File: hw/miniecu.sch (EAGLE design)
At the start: 63 parts

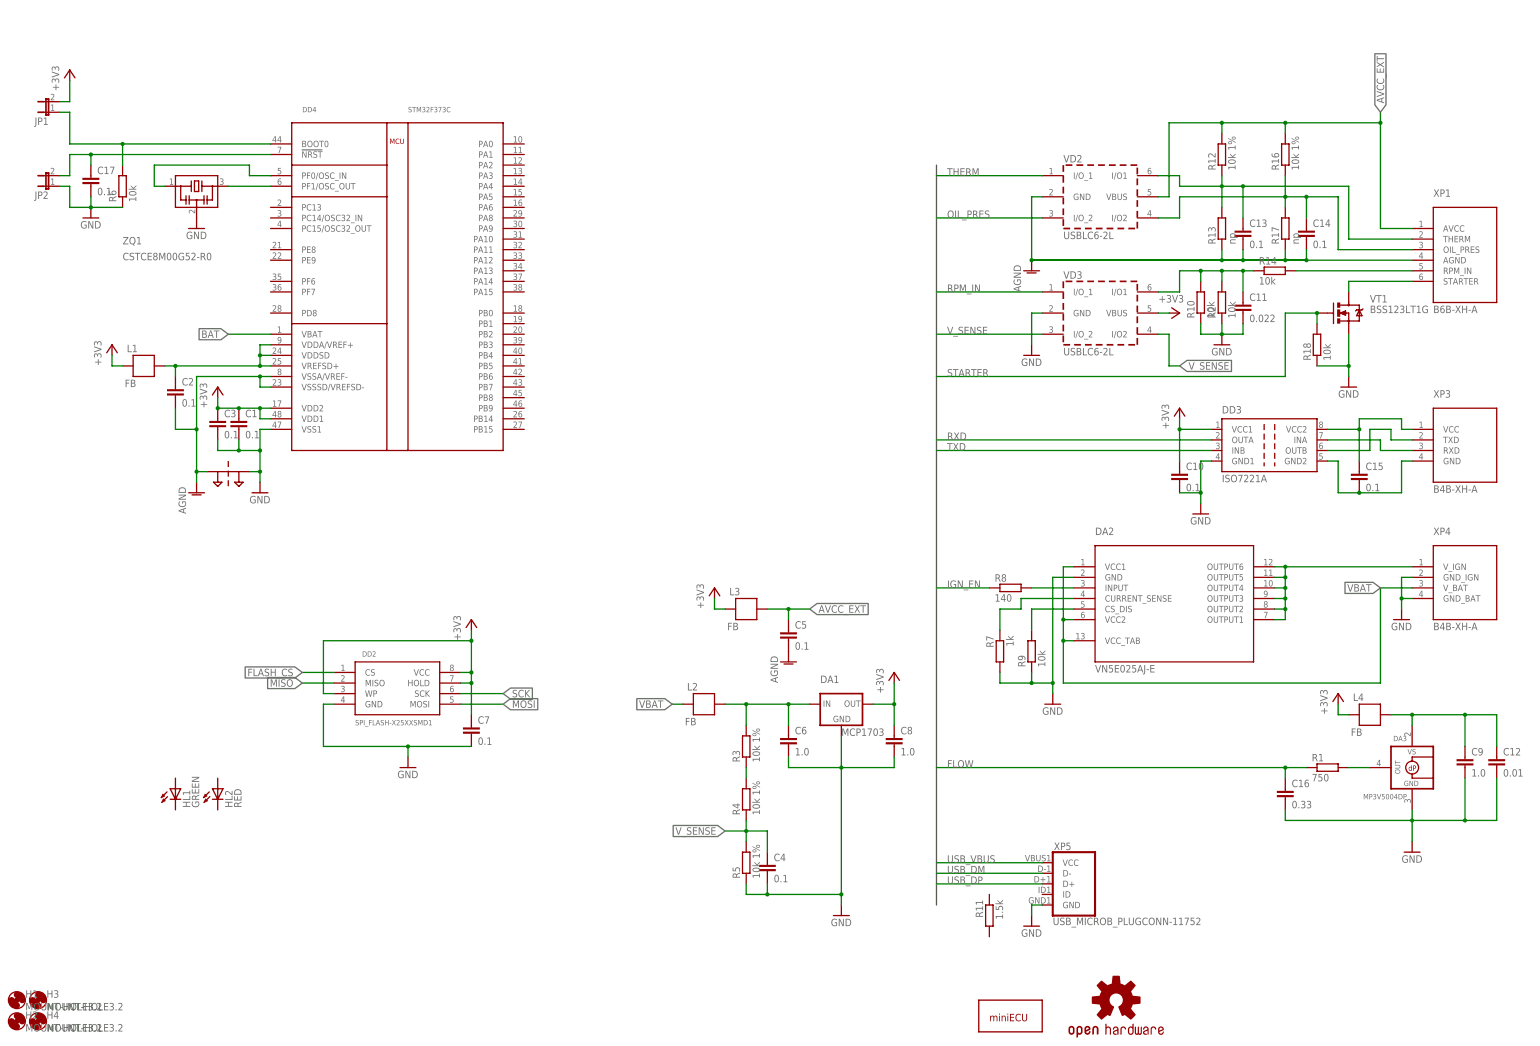
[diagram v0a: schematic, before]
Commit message: hw: do half connections of v2
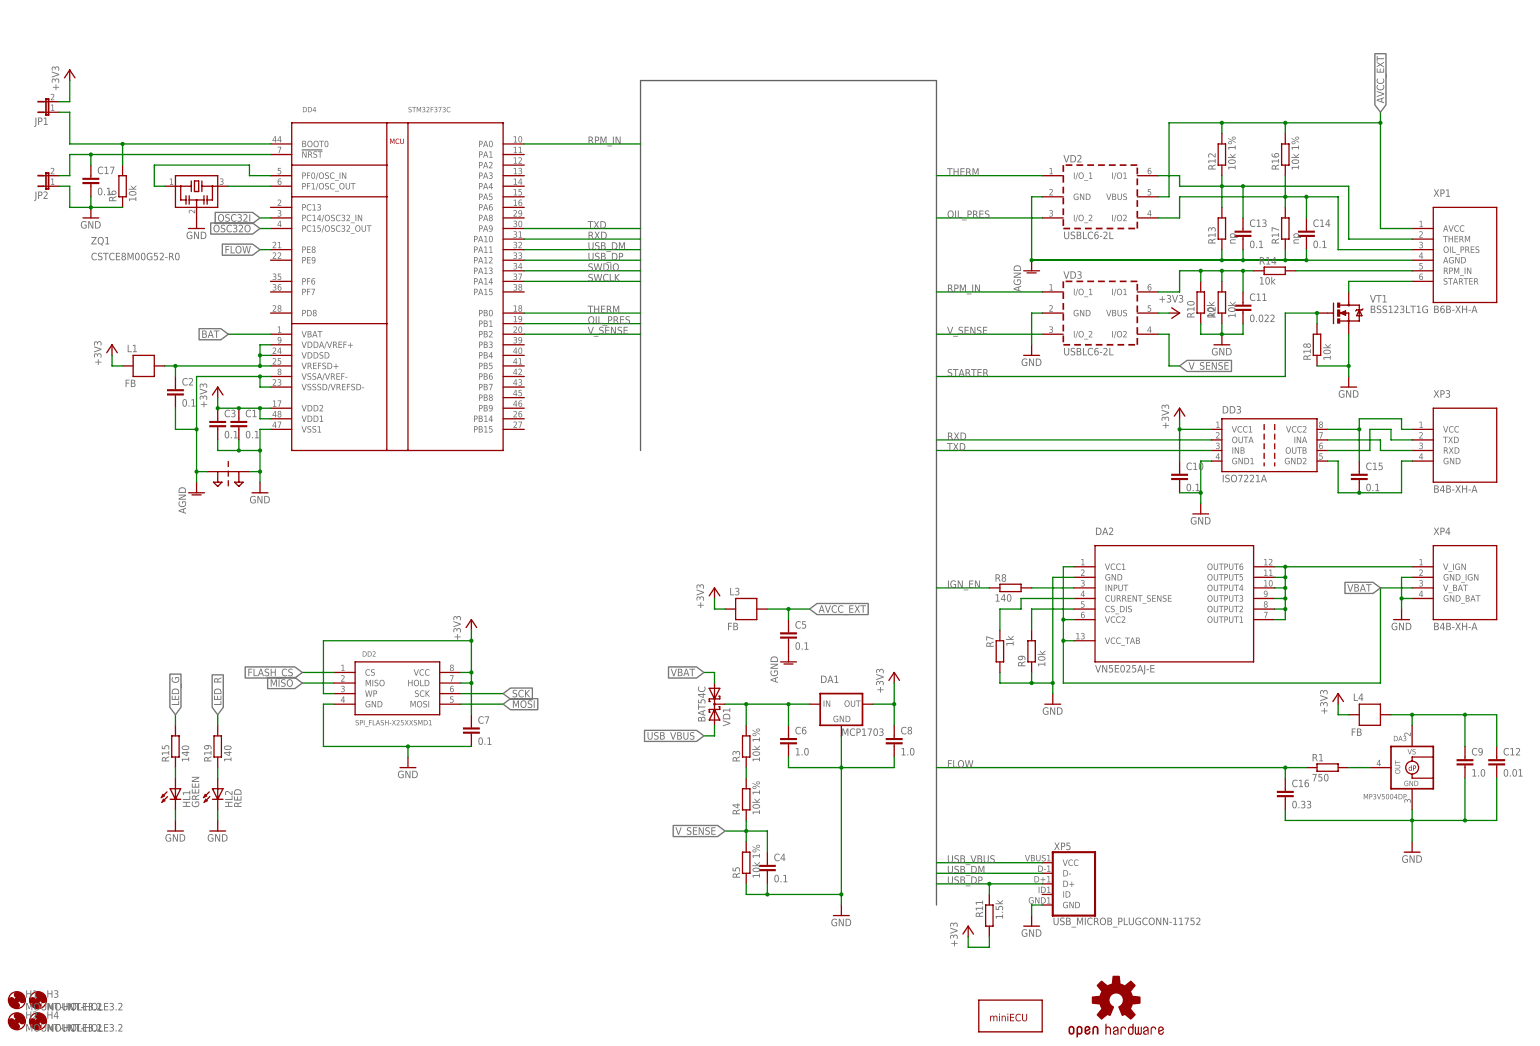
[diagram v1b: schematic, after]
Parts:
- removed L2: FB, SparkFun-Passives:FB
- added R15, R19: 140, resistor:R-EU_R0603
- added VD1: BAT54C, diode:BAT54C
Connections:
- new net LED_G: R15.2
- new net LED_R: R19.2
- new net N$12: HL2.A, R19.1
- new net N$8: HL1.A, R15.1
- new net OSC32I: DD4.PC14/OSC32_IN
- new net OSC32O: DD4.PC15/OSC32_OUT
- new net SWCLK: DD4.PA14
- new net SWDIO: DD4.PA13
- net +3V3: now also R11.2
- net FLOW: now also DD4.PE8
- net GND: now also HL1.C, HL2.C
- net N$6: now also VD1.CC; no longer L2.P$1
- net OIL_PRES: now also DD4.PB1
- net RPM_IN: now also DD4.PA0
- net RXD: now also DD4.PA10
- net THERM: now also DD4.PB0
- net TXD: now also DD4.PA9
- net USB_DM: now also DD4.PA11
- net USB_DP: now also DD4.PA12, R11.1
- net USB_VBUS: now also VD1.A2
- net VBAT: now also VD1.A1; no longer L2.P$2
- net V_SENSE: now also DD4.PB2

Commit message: hw: add SWD, EXT connectors; sch done
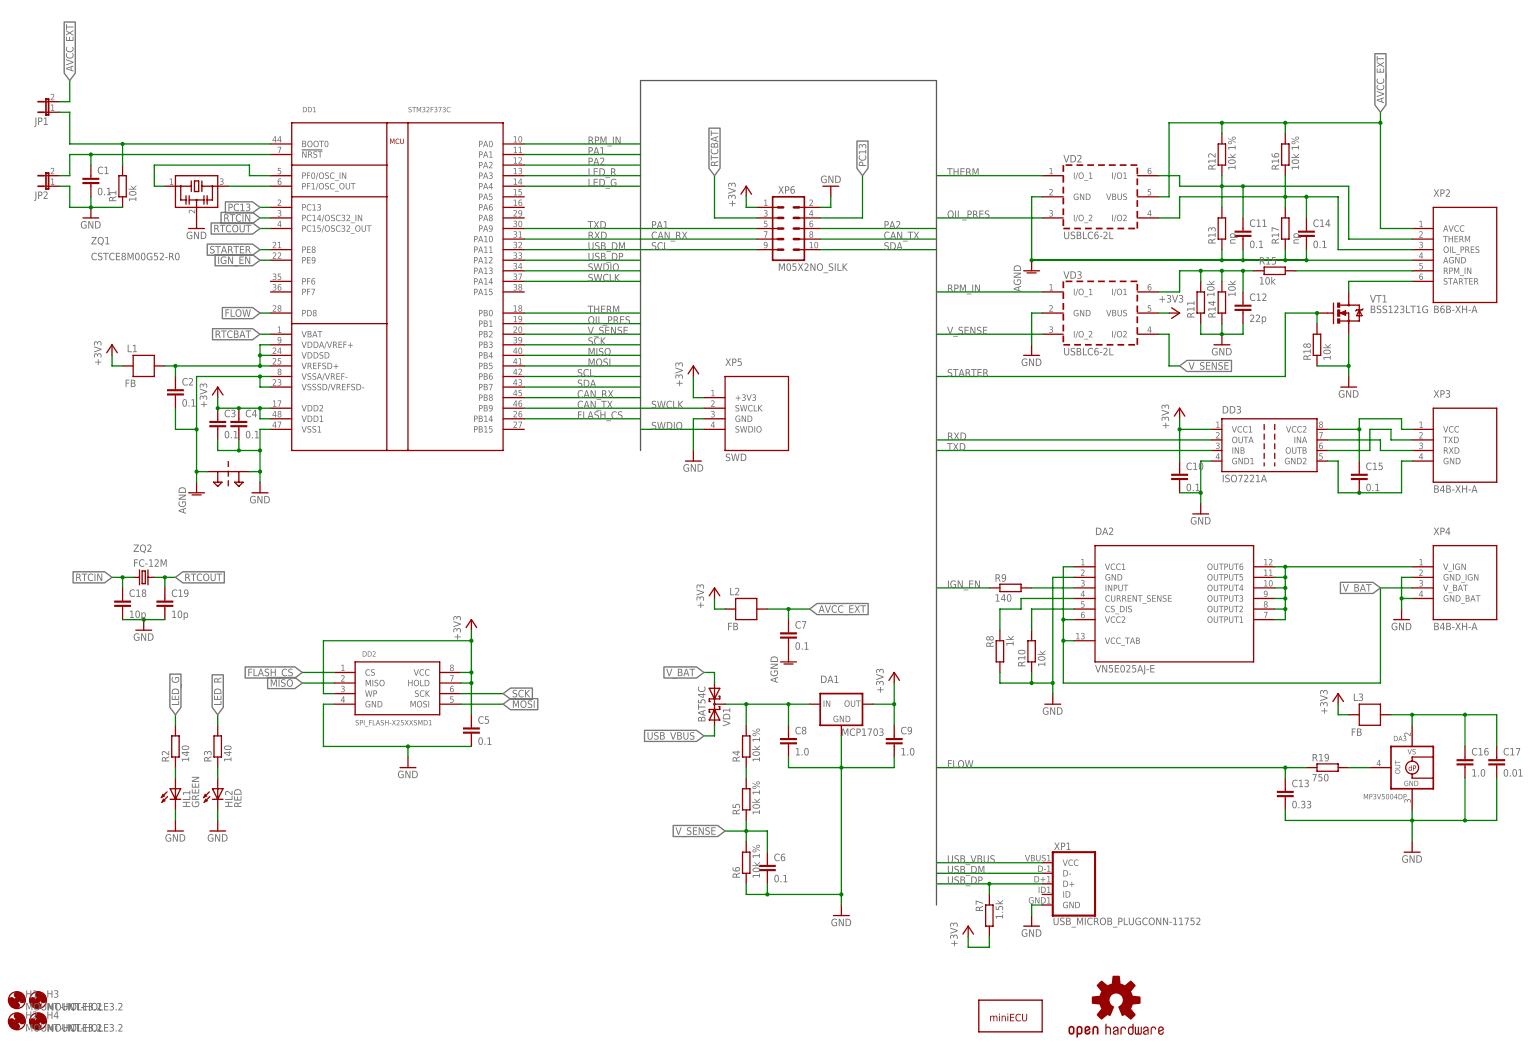
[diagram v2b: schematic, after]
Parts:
- removed L4: FB, SparkFun-Passives:FB
- added C18, C19: 10p, resistor:C-EUC0603
- added L2: FB, SparkFun-Passives:FB
- added XP2: B6B-XH-A, miniecu-con:SENSORS-B6B-XH-A
- added XP6: M05X2NO_SILK, SparkFun-Connectors:M05X2NO_SILK
- added ZQ2: FC-12M, crystal:FC-12M
- C11: value 0.022 -> 0.1
- C12: value 0.01 -> 22p
- C13: value 0.1 -> 0.33
- C16: value 0.33 -> 1.0; device resistor:C-EUC0603 -> resistor:C-EUC0805
- C17: value 0.1 -> 0.01
- C6: value 1.0 -> 0.1; device resistor:C-EUC0805 -> resistor:C-EUC0603
- LOGO1: value OSHW-LOGOL -> MINIECU_LOGO; device SparkFun-Aesthetics:OSHW-LOGOL -> miniecu:MINIECU_LOGO
- LOGO2: value MINIECU_LOGO -> OSHW-LOGOL; device miniecu:MINIECU_LOGO -> SparkFun-Aesthetics:OSHW-LOGOL
- R1: value 750 -> 10k
- R11: value 1.5k -> 10k
- R15: value 140 -> 10k
- R19: value 140 -> 750
- R2, R9: value 10k -> 140
- R3: value 10k 1% -> 140; device resistor:R-EU_R0805 -> resistor:R-EU_R0603
- R6: value 10k -> 10k 1%; device resistor:R-EU_R0603 -> resistor:R-EU_R0805
- R7: value 1k -> 1.5k
- R8: value 140 -> 1k
- XP1: value B6B-XH-A -> USB_MICROB_PLUGCONN-11752; device miniecu-con:SENSORS-B6B-XH-A -> SparkFun-Connectors:USB_MICROB_PLUGCONN-11752
- XP5: value USB_MICROB_PLUGCONN-11752 -> SWD; device SparkFun-Connectors:USB_MICROB_PLUGCONN-11752 -> miniecu-con:SWD
- renumbered DD4 to DD1
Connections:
- net N$5 renamed AVCC
- net VBAT renamed V_BAT
- removed net BAT: DD1.VBAT
- removed net N$10: C17.1, DD1.!NRST, JP2.2
- removed net N$11: DD1.BOOT0, JP1.1, R6.2
- removed net N$3: C12.1, C9.1, DA3.VS, L4.P$1
- removed net OSC32I: DD1.PC14/OSC32_IN
- removed net OSC32O: DD1.PC15/OSC32_OUT
- new net !NRST: C1.1, DD1.!NRST, JP2.2
- new net AVCC_FLOW: C16.1, C17.1, DA3.VS, L3.P$1
- new net BOOT0: DD1.BOOT0, JP1.1, R1.2
- new net CAN_RX: DD1.PB8, XP6.7
- new net CAN_TX: DD1.PB9, XP6.8
- new net PA1: DD1.PA1, XP6.5
- new net PA2: DD1.PA2, XP6.6
- new net PC13: DD1.PC13, XP6.4
- new net RTCBAT: DD1.VBAT, XP6.3
- new net RTCIN: C18.1, DD1.PC14/OSC32_IN, ZQ2.1
- new net RTCOUT: C19.1, DD1.PC15/OSC32_OUT, ZQ2.2
- new net SCL: DD1.PB6, XP6.9
- new net SDA: DD1.PB7, XP6.10
- net +3V3: now also C4.1, C5.1, C9.1, L2.P$2, R7.2, XP5.+3V3, XP6.1; no longer C1.1, C7.1, C8.1, JP1.2, L4.P$2, R11.2
- net AGND: now also C11.2, C7.2, XP2.AGND; no longer C13.2, C5.2, XP1.AGND
- net AVCC_EXT: now also C7.1, JP1.2, L2.P$1, XP2.AVCC; no longer C5.1, L3.P$1, XP1.AVCC
- net FLASH_CS: now also DD1.PB14
- net FLOW: now also C13.1, DD1.PD8, R19.1; no longer C16.1, DD1.PE8, R1.1
- net GND: now also C13.2, C18.2, C19.2, C5.2, R1.1, R11.1, R14.1, R8.2, XP1.GND, XP6.2; no longer C11.2, C7.2, R2.1, R5.1, R7.2, R9.1
- net IGN_EN: now also DD1.PE9, R9.1; no longer R8.1
- net LED_G: now also DD1.PA4, R2.2; no longer R15.2
- net LED_R: now also DD1.PA3, R3.2; no longer R19.2
- net MISO: now also DD1.PB4
- net MOSI: now also DD1.PB5
- net N$1: now also R4.1, R5.2; no longer R3.1, R4.2
- net N$12: now also R3.1; no longer R19.1
- net N$2: now also R8.1; no longer R7.1
- net N$4: now also R19.2; no longer R1.2
- net N$6: now also C8.1, R4.2; no longer C6.1, R3.2
- net N$7: now also R9.2; no longer R8.2
- net N$8: now also R2.1; no longer R15.1
- net N$9: now also R10.2; no longer R9.2
- net OIL_PRES: now also XP2.OIL_PRES; no longer XP1.OIL_PRES
- net RPM_IN: now also C12.1, R11.2, R14.2, R15.1; no longer C11.1, R10.2, R14.1, R2.2
- net RPM_IN_CON: now also R15.2, XP2.RPM_IN; no longer R14.2, XP1.RPM_IN
- net SCK: now also DD1.PB3
- net STARTER: now also DD1.PE8
- net STARTER_OUT: now also XP2.STARTER; no longer XP1.STARTER
- net SWCLK: now also XP5.SWCLK
- net SWDIO: now also XP5.SWDIO
- net THERM: now also C11.1, XP2.THERM; no longer C13.1, XP1.THERM
- net USB_DM: now also XP1.D-; no longer XP5.D-
- net USB_DP: now also R7.1, XP1.D+; no longer R11.1, XP5.D+
- net USB_VBUS: now also XP1.VCC; no longer XP5.VCC
- net V_SENSE: now also C6.1, R5.1, R6.2; no longer C4.1, R4.1, R5.2
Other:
- moved on the sheet: C1, C11, C12, C13, C16, C17, C4, C5, C6, C7, C8, C9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

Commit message: hw: route top half
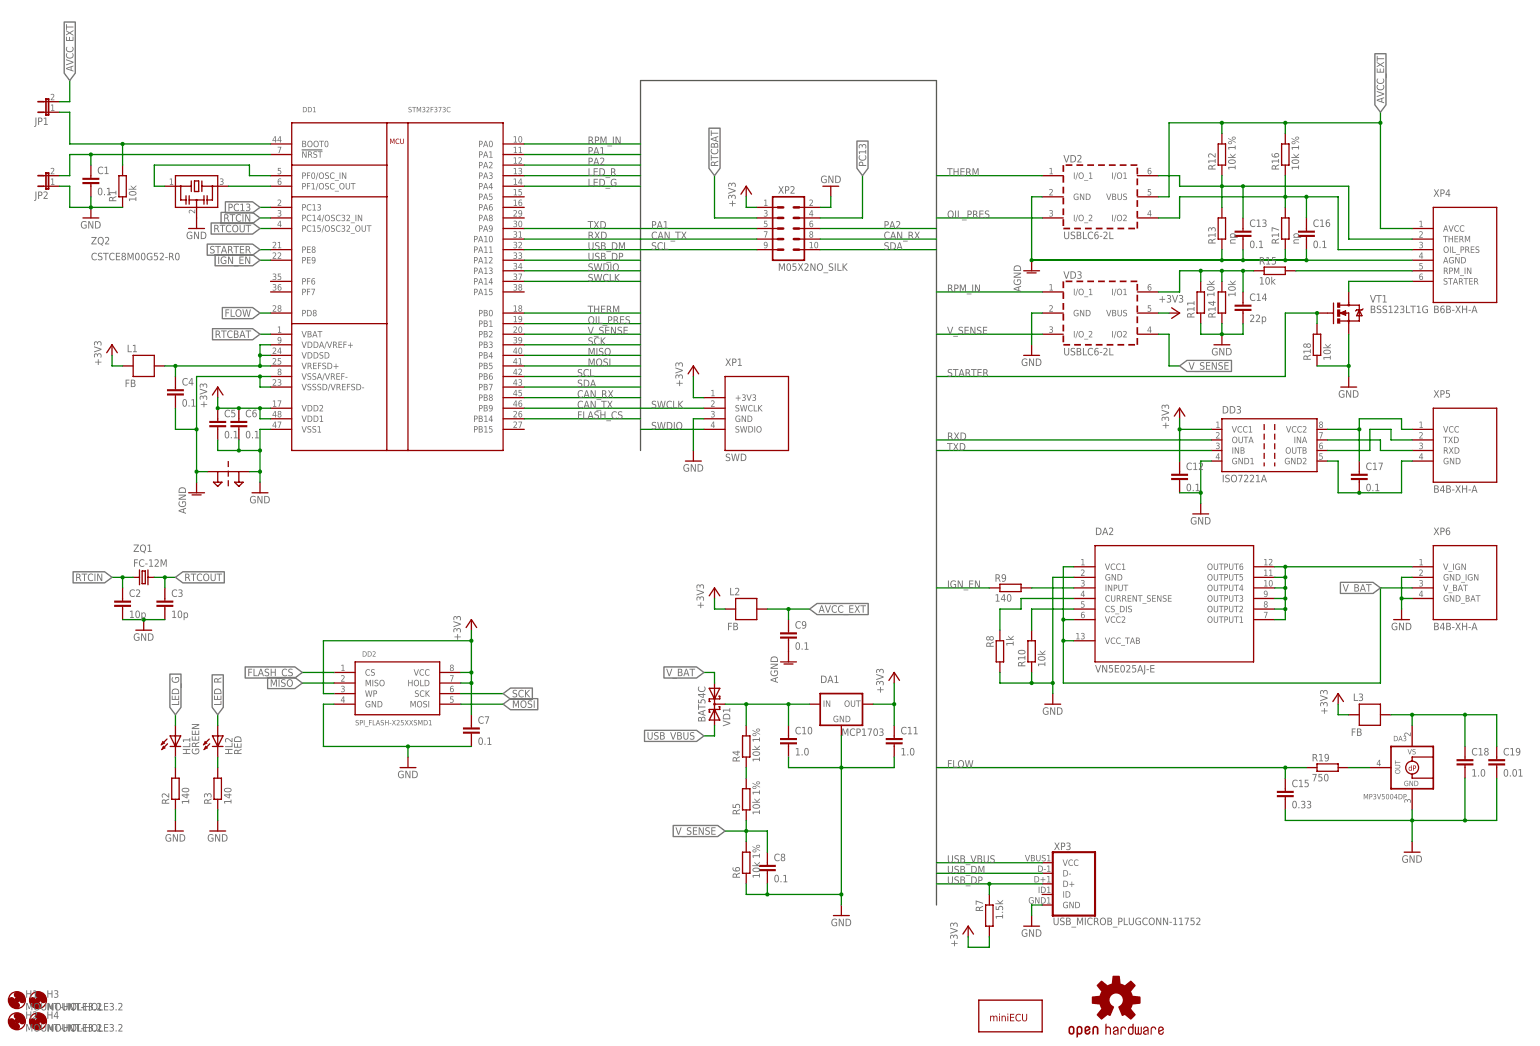
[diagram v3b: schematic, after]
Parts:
- C10, C11: value 0.1 -> 1.0; device resistor:C-EUC0603 -> resistor:C-EUC0805
- C12: value 22p -> 0.1
- C13: value 0.33 -> 0.1
- C14: value 0.1 -> 22p
- C15: value 0.1 -> 0.33
- C16, C8, C9: value 1.0 -> 0.1; device resistor:C-EUC0805 -> resistor:C-EUC0603
- C17: value 0.01 -> 0.1
- C18: value 10p -> 1.0; device resistor:C-EUC0603 -> resistor:C-EUC0805
- C19: value 10p -> 0.01
- C2, C3: value 0.1 -> 10p
- XP1: value USB_MICROB_PLUGCONN-11752 -> SWD; device SparkFun-Connectors:USB_MICROB_PLUGCONN-11752 -> miniecu-con:SWD
- XP2: value B6B-XH-A -> M05X2NO_SILK; device miniecu-con:SENSORS-B6B-XH-A -> SparkFun-Connectors:M05X2NO_SILK
- XP3: value B4B-XH-A -> USB_MICROB_PLUGCONN-11752; device miniecu-con:UART-B4B-XH-A -> SparkFun-Connectors:USB_MICROB_PLUGCONN-11752
- XP4: value B4B-XH-A -> B6B-XH-A; device miniecu-con:IGN_POWER-B4B-XH-A -> miniecu-con:SENSORS-B6B-XH-A
- XP5: value SWD -> B4B-XH-A; device miniecu-con:SWD -> miniecu-con:UART-B4B-XH-A
- XP6: value M05X2NO_SILK -> B4B-XH-A; device SparkFun-Connectors:M05X2NO_SILK -> miniecu-con:IGN_POWER-B4B-XH-A
- ZQ1: value CSTCE8M00G52-R0 -> FC-12M; device cstce-resonator:CSTCE8M00G52-R0 -> crystal:FC-12M
- ZQ2: value FC-12M -> CSTCE8M00G52-R0; device crystal:FC-12M -> cstce-resonator:CSTCE8M00G52-R0
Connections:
- removed net N$12: HL2.A, R3.1
- removed net N$8: HL1.A, R2.1
- new net N$3: HL2.C, R3.2
- new net N$5: HL1.C, R2.2
- net +3V3: now also C11.1, C12.1, C6.1, C7.1, XP1.+3V3, XP2.1; no longer C10.1, C3.1, C4.1, C9.1, XP5.+3V3, XP6.1
- net AGND: now also C13.2, C16.2, C4.2, C9.2, XP4.AGND; no longer C11.2, C14.2, C2.2, C7.2, XP2.AGND
- net AVCC: now also C4.1; no longer C2.1
- net AVCC_EXT: now also C9.1, XP4.AVCC; no longer C7.1, XP2.AVCC
- net AVCC_FLOW: now also C18.1, C19.1; no longer C16.1, C17.1
- net CAN_RX: now also XP2.8; no longer XP6.7
- net CAN_TX: now also XP2.7; no longer XP6.8
- net FLOW: now also C15.1; no longer C13.1
- net GND: now also C11.2, C14.2, C15.2, C2.2, C7.2, R2.1, R3.1, XP2.2, XP3.GND, XP6.GND_BAT, XP6.GND_IGN, ZQ2.2; no longer C13.2, C16.2, C17.2, C4.2, C9.2, HL1.C, HL2.C, XP4.GND_BAT, XP4.GND_IGN, XP5.GND, XP6.2, ZQ1.2
- net GND2: now also C17.2, XP5.GND; no longer C15.2, XP3.GND
- net IORXD: now also XP5.RXD; no longer XP3.RXD
- net IOTXD: now also XP5.TXD; no longer XP3.TXD
- net LED_G: now also HL1.A; no longer R2.2
- net LED_R: now also HL2.A; no longer R3.2
- net N$6: now also C10.1; no longer C8.1
- net OIL_PRES: now also C16.1, XP4.OIL_PRES; no longer C14.1, XP2.OIL_PRES
- net OSC_IN: now also ZQ2.1; no longer ZQ1.1
- net OSC_OUT: now also ZQ2.3; no longer ZQ1.3
- net PA1: now also XP2.5; no longer XP6.5
- net PA2: now also XP2.6; no longer XP6.6
- net PC13: now also XP2.4; no longer XP6.4
- net RPM_IN: now also C14.1; no longer C12.1
- net RPM_IN_CON: now also XP4.RPM_IN; no longer XP2.RPM_IN
- net RTCBAT: now also XP2.3; no longer XP6.3
- net RTCIN: now also C2.1, ZQ1.1; no longer C18.1, ZQ2.1
- net RTCOUT: now also C3.1, ZQ1.2; no longer C19.1, ZQ2.2
- net SCL: now also XP2.9; no longer XP6.9
- net SDA: now also XP2.10; no longer XP6.10
- net STARTER_OUT: now also XP4.STARTER; no longer XP2.STARTER
- net SWCLK: now also XP1.SWCLK; no longer XP5.SWCLK
- net SWDIO: now also XP1.SWDIO; no longer XP5.SWDIO
- net THERM: now also C13.1, XP4.THERM; no longer C11.1, XP2.THERM
- net USB_DM: now also XP3.D-; no longer XP1.D-
- net USB_DP: now also XP3.D+; no longer XP1.D+
- net USB_VBUS: now also XP3.VCC; no longer XP1.VCC
- net VCC2: now also C17.1, XP5.VCC; no longer C15.1, XP3.VCC
- net V_BAT: now also XP6.V_BAT; no longer XP4.V_BAT
- net V_IGN: now also XP6.V_IGN; no longer XP4.V_IGN
- net V_SENSE: now also C8.1; no longer C6.1
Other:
- moved on the sheet: C10, C11, C12, C13, C14, C15, C16, C17, C18, C19, C2, C3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

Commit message: hw: release hw_2.0a
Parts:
- C2, C3: value 10p -> 6p
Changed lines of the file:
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@@
 <part name="+3V11" library="supply1" deviceset="+3V3" device=""/>
 <part name="ZQ1" library="crystal" deviceset="FC-12M" device=""/>
-<part name="C2" library="resistor" deviceset="C-EU" device="C0603" value="10p"/>
-<part name="C3" library="resistor" deviceset="C-EU" device="C0603" value="10p"/>
+<part name="C2" library="resistor" deviceset="C-EU" device="C0603" value="6p"/>
+<part name="C3" library="resistor" deviceset="C-EU" device="C0603" value="6p"/>
 <part name="GND17" library="supply1" deviceset="GND" device=""/>
 <part name="XP2" library="SparkFun-Connectors" deviceset="M05X2" device="NO_SILK"/>
